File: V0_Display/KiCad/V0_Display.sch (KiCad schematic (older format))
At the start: 31 parts, among them J1 USB_B_Micro, J2 I2C Header 1, J3 Conn_01x03, J4 Conn_01x02, J5 SWD Header, J6 I2C Header 2, J7 USB_Header, J8 Conn_01x02, SW1 SW_SPST, SW2 SW_SPST, SW3 SW_SPST, SW4 SW_SPST, SW5 SW_SPST, SW6 SW_SPST, SW7 Rotary_Encoder_Switch, U1 AP2127K-3.3, U2 STM32F042F6Px, U3 74LVC1G17

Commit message: Library Localization and Pinout changes
Added Selection jumpers for pins 1 and 2 on OLED header (Power and Ground) for use with different OLED pinouts.

Moved all footprints, schematic symbols and 3D models to the V0 folder for simplification
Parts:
- removed J6: I2C Header 2, Connector_PinHeader_2.54mm:PinHeader_1x04_P2.54mm_Vertical, symbol Connector_Generic:Conn_01x04
- added JP1: Pin2, V0-Display:SolderJumper-3_P1.3mm_Bridged12_Pad1.0x1.5mm, symbol V0_Display:SolderJumper_3_Bridged12
- added JP2: Pin1, V0-Display:SolderJumper-3_P1.3mm_Bridged12_Pad1.0x1.5mm, symbol V0_Display:SolderJumper_3_Bridged12
- C1, C2: footprint Capacitor_SMD:C_0805_2012Metric -> V0-Display:C_0805_2012Metric
- C3, C4: footprint Capacitor_SMD:C_0805_2012Metric -> V0-Display:C_0805_2012Metric; symbol Device:C -> V0_Display:C
- D1: footprint LED_SMD:LED_WS2812B_PLCC4_5.0x5.0mm_P3.2mm -> V0-Display:LED_WS2812B_PLCC4_5.0x5.0mm_P3.2mm; symbol LED:WS2812B -> V0_Display:WS2812B
- GPIO1: footprint Connector_PinHeader_2.54mm:PinHeader_1x03_P2.54mm_Horizontal -> V0-Display:PinHeader_1x03_P2.54mm_Vertical; symbol Connector_Generic:Conn_01x03 -> V0_Display:Conn_01x03
- H1, H2, H3, H4: footprint MountingHole:MountingHole_3.2mm_M3 -> V0-Display:MountingHole_3.2mm_M3; symbol Mechanical:MountingHole -> V0_Display:MountingHole
- J1: footprint TRA_KiCad_Footprints:MolexVertical&Horizontal_MicroB -> V0-Display:MolexVertical&Horizontal_MicroB; symbol Connector:USB_B_Micro -> V0_Display:USB_B_Micro
- J2: footprint TRA_KiCad_Footprints:1pt3in_OLED -> V0-Display:1pt3in_OLED; symbol Connector_Generic:Conn_01x04 -> V0_Display:Conn_01x04
- J3: footprint Connector_PinHeader_2.54mm:PinHeader_1x03_P2.54mm_Vertical -> V0-Display:PinHeader_1x03_P2.54mm_Vertical; symbol Connector_Generic:Conn_01x03 -> V0_Display:Conn_01x03
- J4, J8: footprint Connector_PinHeader_2.54mm:PinHeader_1x02_P2.54mm_Vertical -> V0-Display:PinHeader_1x02_P2.54mm_Vertical; symbol Connector_Generic:Conn_01x02 -> V0_Display:Conn_01x02
- J5: footprint Connector_PinHeader_1.27mm:PinHeader_2x05_P1.27mm_Vertical_SMD -> V0-Display:PinHeader_2x05_P1.27mm_Vertical_SMD; symbol Connector_Generic:Conn_02x05_Odd_Even -> V0_Display:Conn_02x05_Odd_Even
- J7: footprint TRA_KiCad_Footprints:01x04_unpopulated -> V0-Display:PinHeader_1x04_P2.54mm_Vertical; symbol Connector_Generic:Conn_01x04 -> V0_Display:Conn_01x04
- R1, R2, R3: footprint Resistor_SMD:R_0805_2012Metric -> V0-Display:R_0805_2012Metric; symbol Device:R -> V0_Display:R
- SW1, SW2, SW3, SW4: footprint Button_Switch_THT:SW_PUSH_6mm_H9.5mm -> V0-Display:SW_PUSH_6mm; symbol Switch:SW_SPST -> V0_Display:SW_SPST
- SW5: footprint Button_Switch_THT:SW_PUSH_6mm -> V0-Display:SW_PUSH_6mm
- SW6: footprint Button_Switch_THT:SW_PUSH_6mm -> V0-Display:SW_PUSH_6mm; symbol Switch:SW_SPST -> V0_Display:SW_SPST
- SW7: footprint TRA_KiCad_Footprints:EN11_Encoder -> V0-Display:EN11_Encoder; symbol Device:Rotary_Encoder_Switch -> V0_Display:Rotary_Encoder_Switch
- U1: footprint Package_TO_SOT_SMD:SOT-23-5 -> V0-Display:SOT-23-5; symbol Regulator_Linear:AP2127K-3.3 -> V0_Display:AP2127K-3.3
- U2: footprint Package_SO:TSSOP-20_4.4x6.5mm_P0.65mm -> V0-Display:TSSOP-20_4.4x6.5mm_P0.65mm; symbol MCU_ST_STM32F0:STM32F042F6Px -> V0_Display:STM32F042F6Px
- U3: footprint digikey-footprints:SOT-753 -> V0-Display:SOT-753; symbol 74xGxx:74LVC1G17 -> V0_Display:74LVC1G17
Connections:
- net +3V3: now also JP1.1 (A), JP2.3 (B); no longer J2.2 (Pin_2)
- net GND: now also JP1.3 (B), JP2.1 (A); no longer J2.1 (Pin_1)
- new net Pin1: J2.1 (Pin_1), JP2.2 (C)
- new net Pin2: J2.2 (Pin_2), JP1.2 (C)
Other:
- moved on the sheet: H1, H2, H3, H4, J2, J3, R3, SW7

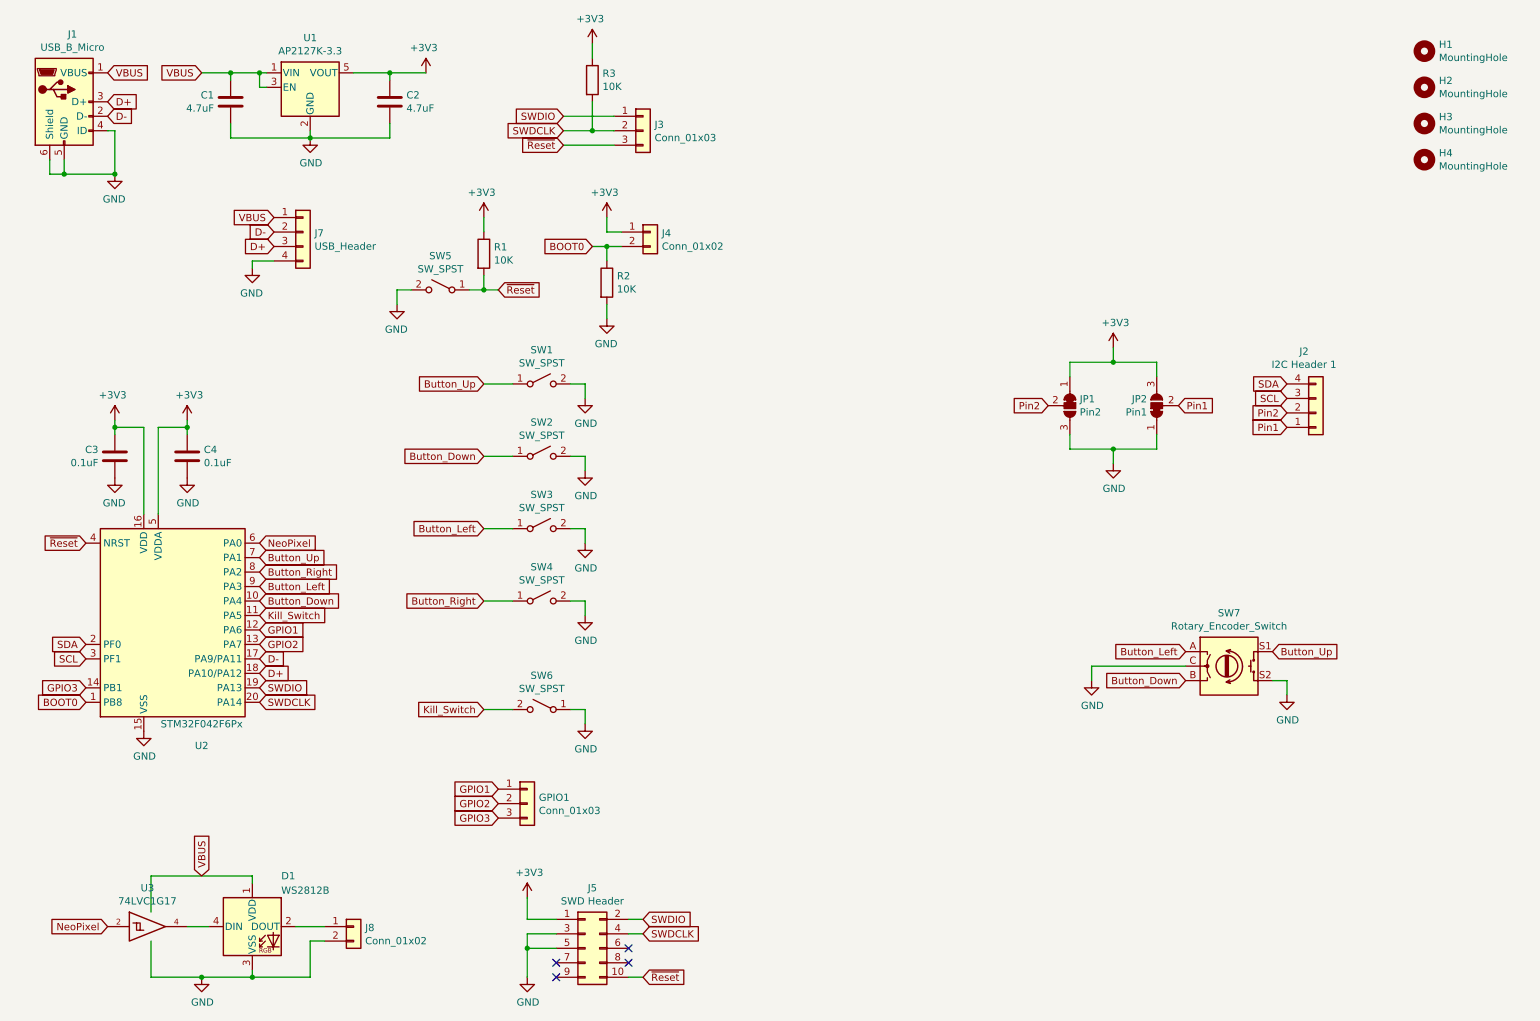
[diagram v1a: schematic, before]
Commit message: Removal of control buttons
No-one used them, why have them on the board?
Removed 4 directional buttons
Updates of documentation
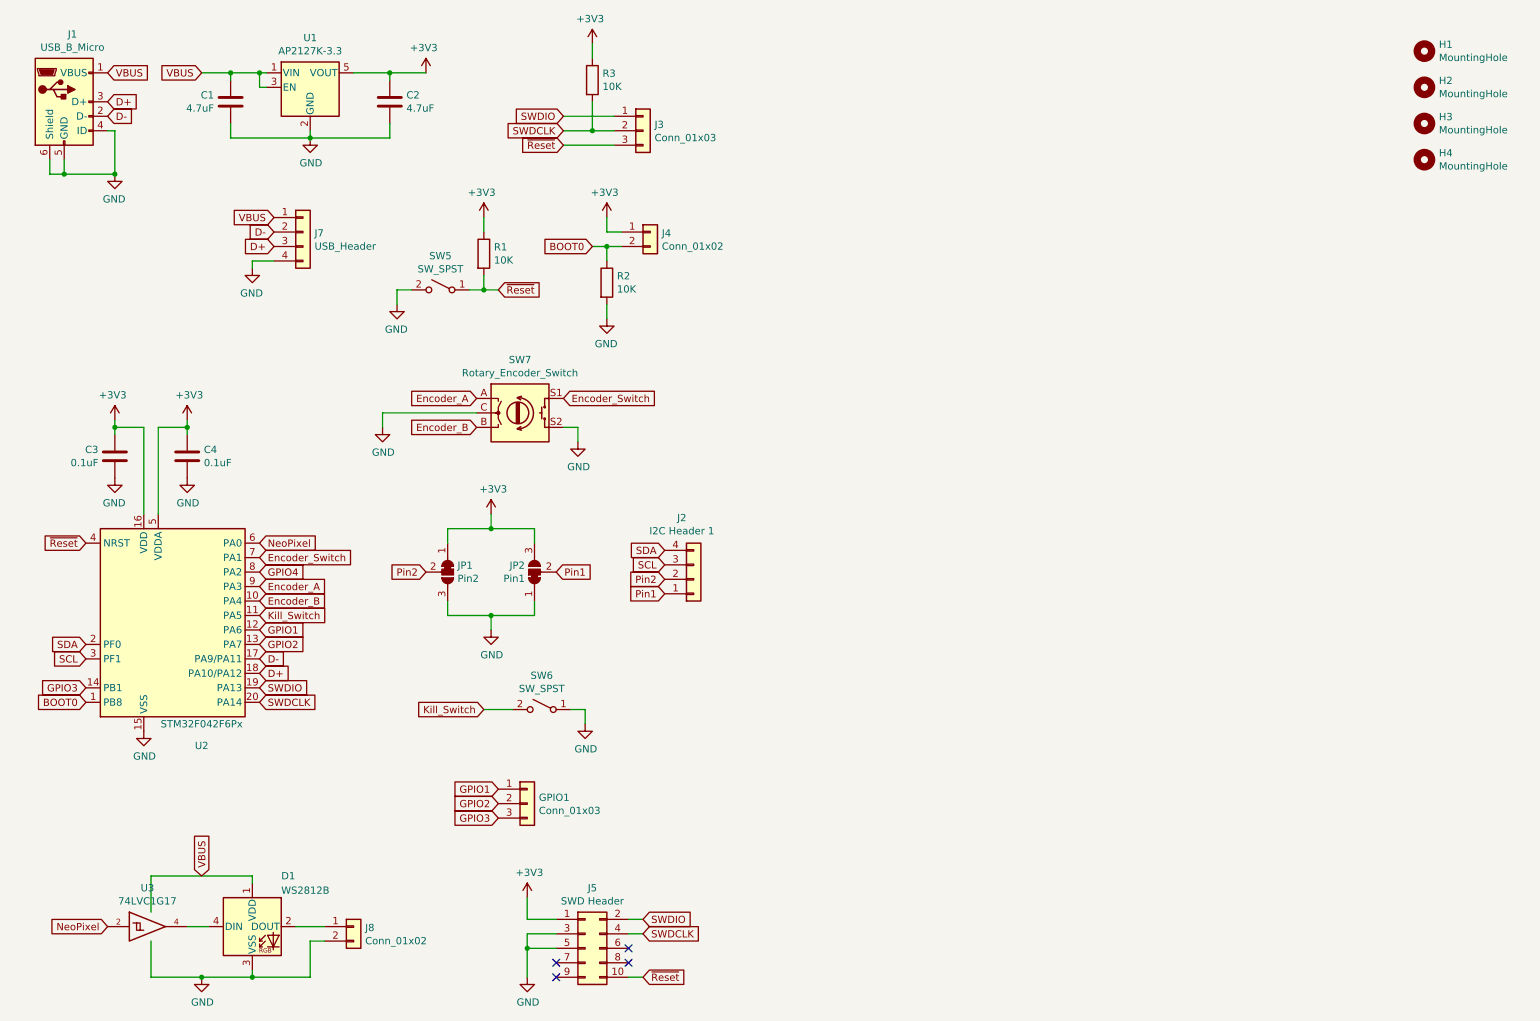
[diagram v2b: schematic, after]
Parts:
- removed SW1, SW2, SW3, SW4: SW_SPST, V0-Display:SW_PUSH_6mm, symbol V0_Display:SW_SPST
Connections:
- net Button_Down renamed Encoder_B
- net Button_Left renamed Encoder_A
- net Button_Right renamed GPIO4
- net Button_Up renamed Encoder_Switch
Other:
- moved on the sheet: J2, JP1, JP2, SW7
